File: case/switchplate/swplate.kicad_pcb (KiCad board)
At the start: 2 copper layers, 340 x 131 mm, 12 parts

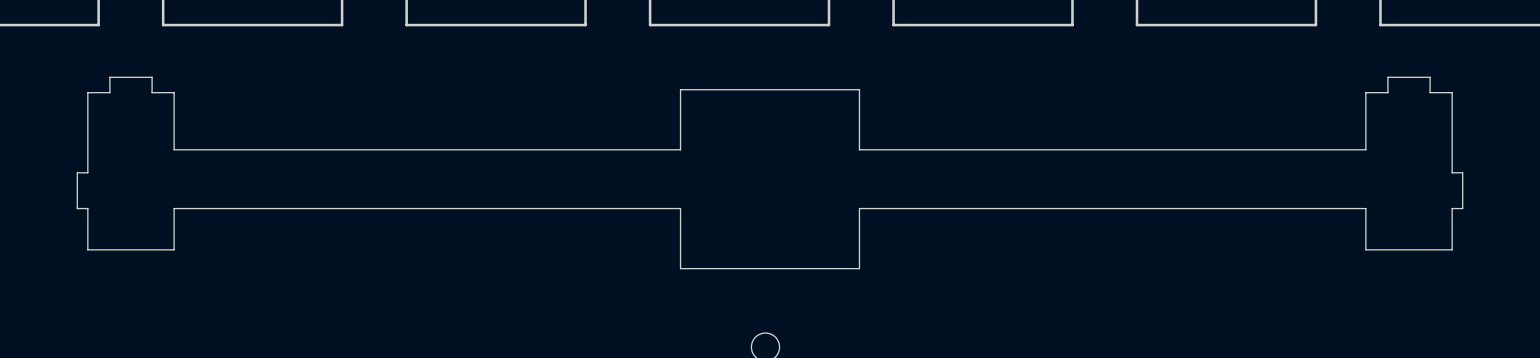
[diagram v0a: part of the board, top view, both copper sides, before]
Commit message: Finished case, minor changes to PCB, laser cutting files prepped
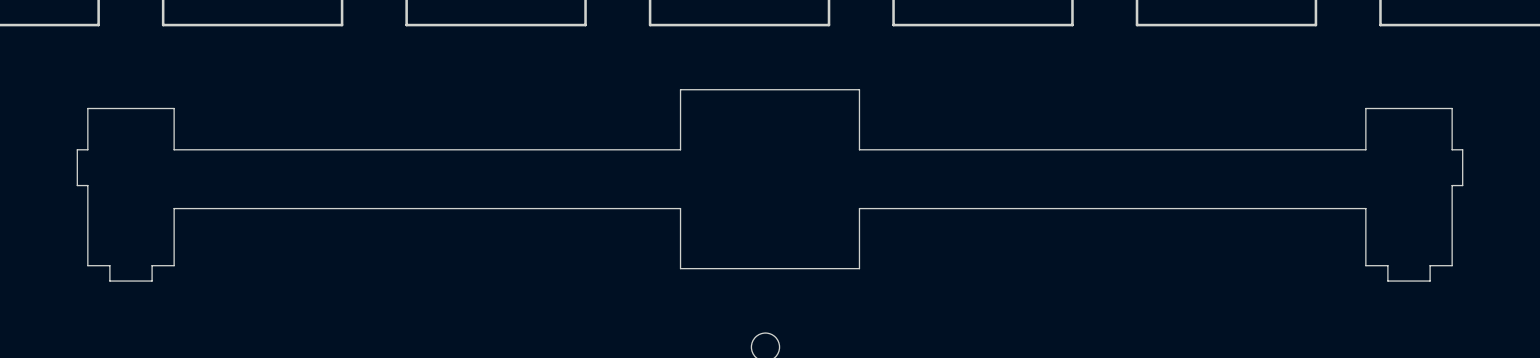
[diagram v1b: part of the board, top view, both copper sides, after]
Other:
- outline, holes or cut-outs redrawn
